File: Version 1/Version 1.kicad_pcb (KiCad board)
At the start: 2 copper layers, 97.2 x 106 mm, 77 parts, among them J1 Conn_01x05, Q1 IPP015N04NF2SAKMA1, Q2 IPP015N04NF2SAKMA1, Q3 IPP015N04NF2SAKMA1, Q4 IPP015N04NF2SAKMA1, Q5 IPP015N04NF2SAKMA1, Q6 IPP015N04NF2SAKMA1, U1 TPS62932, U2 TPS62932, U3 TPS62932, U4 IRS2004, U5 IRS2004, U6 IRS2004, U7 YAAJ_BlackPill_SWD_BreakoutV2, U8 Conn_01x01_Socket

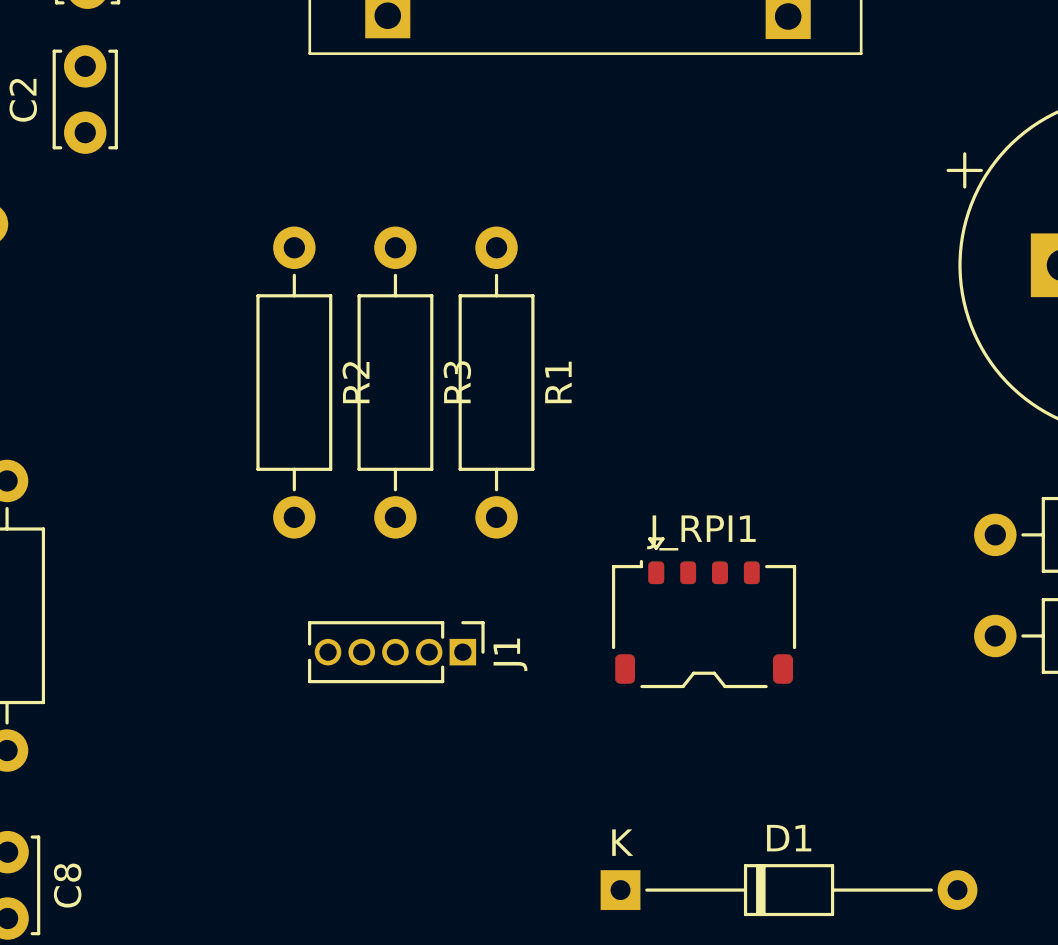
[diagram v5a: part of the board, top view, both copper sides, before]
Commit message: updated footprints and added pos in pcb design
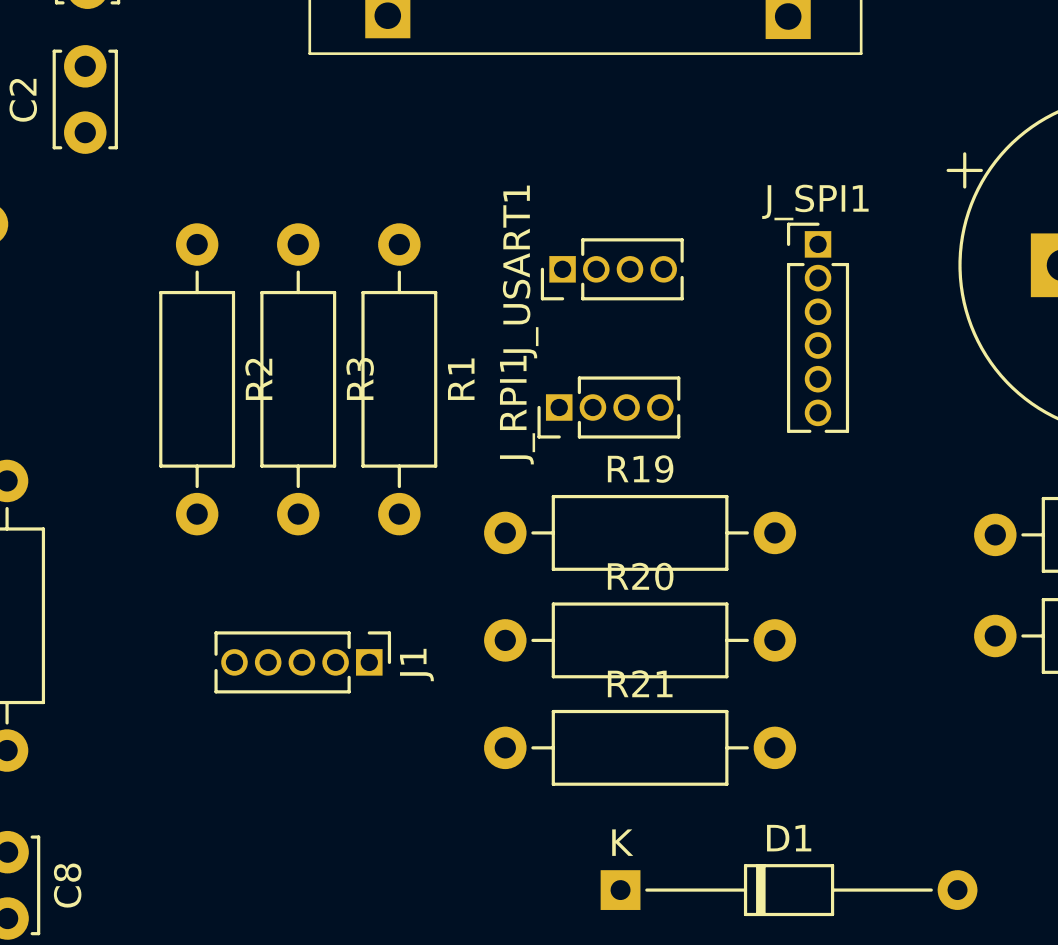
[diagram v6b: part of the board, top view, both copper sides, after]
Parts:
- added J_SPI1: Conn_01x06, Connector_PinHeader_1.27mm:PinHeader_1x06_P1.27mm_Vertical, F.Cu at (74.8, 79.1)
- added J_USART1: Conn_01x04, Connector_PinHeader_1.27mm:PinHeader_1x04_P1.27mm_Vertical, F.Cu at (65.2, 80.1)
- added R19: 1k5, Resistor_THT:R_Axial_DIN0207_L6.3mm_D2.5mm_P10.16mm_Horizontal, F.Cu at (63.0, 90.0)
- added R20: 1k5, Resistor_THT:R_Axial_DIN0207_L6.3mm_D2.5mm_P10.16mm_Horizontal, F.Cu at (63.0, 94.1)
- added R21: 10k, Resistor_THT:R_Axial_DIN0207_L6.3mm_D2.5mm_P10.16mm_Horizontal, F.Cu at (63.0, 98.1)
- J_RPI1: footprint Connector_JST:JST_ACH_BM04B-ACHSS-A-GAN-ETF_1x04-1MP_P1.20mm_Vertical -> Connector_PinHeader_1.27mm:PinHeader_1x04_P1.27mm_Vertical
- moved J_RPI1 9.77 mm to (65.0, 85.3), turned to 90 degrees
- moved R3 3.66 mm to (55.2, 79.2)
- moved R1 3.66 mm to (59.0, 79.2)
- moved R2 3.66 mm to (51.4, 79.2)
- moved J1 3.55 mm to (57.9, 94.9)
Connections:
- U7 pad 10: unconnected-(U7-A4-Pad10) -> ADC2
- U7 pad 11: unconnected-(U7-A5-Pad11) -> ADC3
- U7 pad 13: IN_V -> SPI_MOSI
- U7 pad 14: IN_W -> IN_V
- U7 pad 15: unconnected-(U7-B1-Pad15) -> T1_WN
- U7 pad 16: unconnected-(U7-B2-Pad16) -> B2
- U7 pad 21: unconnected-(U7-B12-Pad21) -> B12
- U7 pad 22: unconnected-(U7-B13-Pad22) -> T1_UN
- U7 pad 23: unconnected-(U7-B14-Pad23) -> T1_VN
- U7 pad 24: unconnected-(U7-B15-Pad24) -> B15
- U7 pad 25: unconnected-(U7-A8-Pad25) -> T1_U
- U7 pad 26: unconnected-(U7-A9-Pad26) -> T1_V
- U7 pad 27: unconnected-(U7-A10-Pad27) -> T1_W
- U7 pad 28: unconnected-(U7-A11-Pad28) -> USART6_TX
- U7 pad 29: unconnected-(U7-A12-Pad29) -> USART6_RX
- U7 pad 30: unconnected-(U7-A15-Pad30) -> SPI_CS1
- U7 pad 31: SDA_RPI -> SPI_SCK
- U7 pad 32: unconnected-(U7-B4-Pad32) -> SPI_MISO
- U7 pad 33: HallU -> IN_W
- U7 pad 34: HallV -> HallU
- U7 pad 35: HallW -> HallV
- U7 pad 36: unconnected-(U7-B8-Pad36) -> HallW
- U7 pad 37: unconnected-(U7-B9-Pad37) -> SDA_RPI
- U7 pad 5: unconnected-(U7-R-Pad5) -> Reset
- U7 pad 6: unconnected-(U7-A0-Pad6) -> HSM_U
- U7 pad 7: unconnected-(U7-A1-Pad7) -> HSM_V
- U7 pad 8: unconnected-(U7-A2-Pad8) -> HSM_W
- U7 pad 9: unconnected-(U7-A3-Pad9) -> ADC1
